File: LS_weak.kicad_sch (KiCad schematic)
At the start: 12 parts, among them Q10 AO3400A, Q11 AO3400A, Q24 AO3400A, Q27 AO3400A

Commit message: Export
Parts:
- removed D49: PSM712-LF, hellen-one-common:SOT-23, symbol Power_Management:PSM712
- added D29: PSM712, hellen-one-common:SOT-23, symbol hellen-one-common:PSM712
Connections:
- net GND: now also D29.2
- net OUT4 (ALWAYS_HOT): now also D29.1
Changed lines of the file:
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@@
         )
         (path "/63d2dd9f-d5ff-4811-a88d-0ba932475460/d86ecd12-d50a-4fcf-baad-7cff6bac9c13"
-          (reference "#PWR0139") (unit 1)
+          (reference "#PWR0184") (unit 1)
         )
       )
@@
         )
         (path "/63d2dd9f-d5ff-4811-a88d-0ba932475460/d86ecd12-d50a-4fcf-baad-7cff6bac9c13"
-          (reference "#PWR0145") (unit 1)
+          (reference "#PWR0200") (unit 1)
         )
       )
@@
         )
         (path "/63d2dd9f-d5ff-4811-a88d-0ba932475460/d86ecd12-d50a-4fcf-baad-7cff6bac9c13"
-          (reference "#PWR0141") (unit 1)
+          (reference "#PWR0199") (unit 1)
         )
       )
@@
         )
         (path "/63d2dd9f-d5ff-4811-a88d-0ba932475460/d86ecd12-d50a-4fcf-baad-7cff6bac9c13"
-          (reference "#PWR0142") (unit 1)
+          (reference "#PWR0198") (unit 1)
         )
       )
@@
         )
         (path "/63d2dd9f-d5ff-4811-a88d-0ba932475460/d86ecd12-d50a-4fcf-baad-7cff6bac9c13"
-          (reference "#PWR0144") (unit 1)
+          (reference "#PWR0195") (unit 1)
+        )
+      )
+    )
+  )
+  (symbol (lib_id "hellen-one-common:PSM712") (at 130.556 163.83 0) (unit 1)
+    (in_bom yes) (on_board yes) (dnp no) (fields_autoplaced)
+    (property "Reference" "D29" (at 134.366 162.56 0)
+      (effects (font (size 1.27 1.27)) (justify left))
+    )
+    (property "Value" "PSM712" (at 134.366 165.1 0)
+      (effects (font (size 1.27 1.27)) (justify left))
+    )
+    (property "Footprint" "hellen-one-common:SOT-23" (at 130.302 169.926 0)
+      (effects (font (size 1.27 1.27) italic) hide)
+    )
+    (property "Datasheet" "https://datasheet.lcsc.com/lcsc/1811061632_ProTek-Devices-PSM712-LF-T7_C32677.pdf" (at 128.016 168.656 0)
+      (effects (font (size 1.27 1.27)) hide)
+    )
+    (property "LCSC" "C32677" (at 121.158 171.704 0)
+      (effects (font (size 1.27 1.27)) hide)
+    )
+    (pin "1")
+    (pin "2")
+    (pin "3")
+    (instances
+      (project "alphax_4ch"
+        (path "/63d2dd9f-d5ff-4811-a88d-0ba932475460/d86ecd12-d50a-4fcf-baad-7cff6bac9c13"
+          (reference "D29") (unit 1)
         )
       )
@@
         )
         (path "/63d2dd9f-d5ff-4811-a88d-0ba932475460/d86ecd12-d50a-4fcf-baad-7cff6bac9c13"
-          (reference "#PWR0147") (unit 1)
+          (reference "#PWR0183") (unit 1)
         )
       )
@@
         )
         (path "/63d2dd9f-d5ff-4811-a88d-0ba932475460/d86ecd12-d50a-4fcf-baad-7cff6bac9c13"
-          (reference "#PWR0146") (unit 1)
-        )
-      )
-    )
-  )
-  (symbol (lib_id "Power_Management:PSM712") (at 130.556 163.83 0) (unit 1)
-    (in_bom yes) (on_board yes) (dnp no) (fields_autoplaced)
-    (property "Reference" "D49" (at 133.858 162.9215 0)
-      (effects (font (size 1.27 1.27)) (justify left))
-    )
-    (property "Value" "PSM712-LF" (at 133.858 165.6966 0)
-      (effects (font (size 1.27 1.27)) (justify left))
-    )
-    (property "Footprint" "hellen-one-common:SOT-23" (at 130.302 169.926 0)
-      (effects (font (size 1.27 1.27) italic) hide)
-    )
-    (property "Datasheet" "https://datasheet.lcsc.com/lcsc/1811061632_ProTek-Devices-PSM712-LF-T7_C32677.pdf" (at 128.016 168.656 0)
-      (effects (font (size 1.27 1.27)) hide)
-    )
-    (property "LCSC" "C32677" (at 121.158 171.704 0)
-      (effects (font (size 1.27 1.27)) hide)
-    )
-    (pin "1")
-    (pin "2")
-    (pin "3")
-    (instances
-      (project "alphax_4ch"
-        (path "/63d2dd9f-d5ff-4811-a88d-0ba932475460"
-          (reference "D49") (unit 1)
-        )
-        (path "/63d2dd9f-d5ff-4811-a88d-0ba932475460/d86ecd12-d50a-4fcf-baad-7cff6bac9c13"
-          (reference "D29") (unit 1)
+          (reference "#PWR0194") (unit 1)
         )
       )
@@
         )
         (path "/63d2dd9f-d5ff-4811-a88d-0ba932475460/d86ecd12-d50a-4fcf-baad-7cff6bac9c13"
-          (reference "#PWR0143") (unit 1)
+          (reference "#PWR0197") (unit 1)
         )
       )
@@
         )
         (path "/63d2dd9f-d5ff-4811-a88d-0ba932475460/d86ecd12-d50a-4fcf-baad-7cff6bac9c13"
-          (reference "#PWR0148") (unit 1)
-        )
-      )
+          (reference "#PWR0196") (unit 1)
+        )
+      )

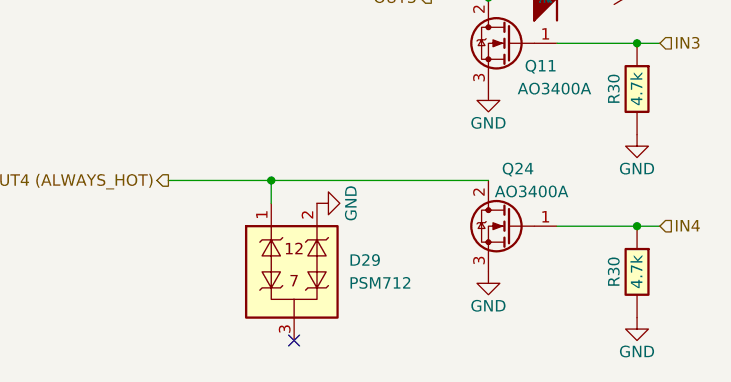
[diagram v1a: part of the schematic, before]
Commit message: PSM712-LF value fix
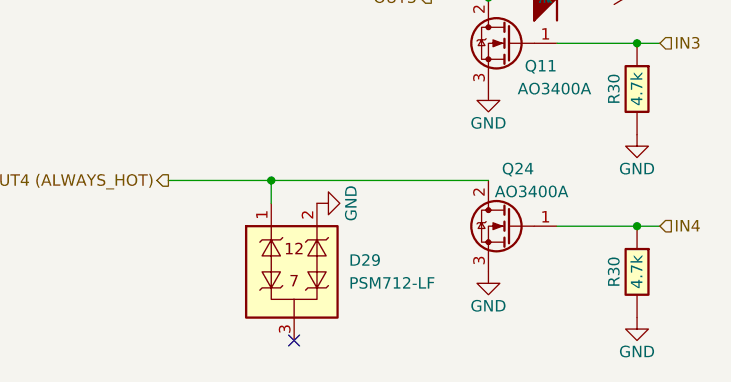
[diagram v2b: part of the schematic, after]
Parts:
- D29: value PSM712 -> PSM712-LF
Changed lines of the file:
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@@
       (effects (font (size 1.27 1.27)) (justify left))
     )
-    (property "Value" "PSM712" (at 134.366 165.1 0)
+    (property "Value" "PSM712-LF" (at 134.366 165.1 0)
       (effects (font (size 1.27 1.27)) (justify left))
     )
